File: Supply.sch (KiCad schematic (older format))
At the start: 27 parts, among them IC1 LM5017, IC2 AP65111, U6 7805_SO8

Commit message: - removed lots of unused circuitry - implemented new DMOS power stage - power supplies still missing - removed rescue lib and fixed referenced
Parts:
- removed C10, C45, C48: 22u, Capacitor_SMD:C_0805_2012Metric, symbol Device:C
- removed C11, C12, C27, C31, C32: 100n, Capacitor_SMD:C_0805_2012Metric, symbol Device:C
- removed C28: 100n, Capacitor_SMD:C_0805_2012Metric, symbol Device:C_Small
- removed C30: 1u, Capacitor_SMD:C_1206_3216Metric, symbol Device:C
- removed C46: 3n3, Capacitor_SMD:C_0805_2012Metric, symbol Device:C_Small
- removed C49: 100u 22V, Capacitor_THT:CP_Radial_D6.3mm_P2.50mm, symbol Device:CP
- removed D8: 4148, Diode_SMD:D_MiniMELF, symbol Device:D_Small
- removed IC1: LM5017, Package_SO:HSOP-8-1EP_3.9x4.9mm_P1.27mm_EP2.41x3.1mm, symbol Revolter-rescue:LM5017
- removed IC2: AP65111, Package_TO_SOT_SMD:SOT-23-6, symbol Revolter-rescue:AP65111
- removed L1: VLS6045EX-221M, Inductor_SMD:L_Taiyo-Yuden_NR-60xx_HandSoldering, symbol Revolter-rescue:INDUCTOR
- removed L2: NRH2410T100MN, Inductor_SMD:L_Taiyo-Yuden_NR-24xx_HandSoldering, symbol Revolter-rescue:INDUCTOR_SMALL
- removed R30: 82k, Resistor_SMD:R_0805_2012Metric, symbol Device:R
- removed R31, R44: 10k, Resistor_SMD:R_0805_2012Metric, symbol Device:R
- removed R39: 499k, Resistor_SMD:R_0805_2012Metric, symbol Device:R
- removed R40: 59k, Resistor_SMD:R_0805_2012Metric, symbol Device:R
- removed R41: 46k4, Resistor_SMD:R_0805_2012Metric, symbol Device:R
- removed R42: 40k2, Resistor_SMD:R_0805_2012Metric, symbol Device:R
- removed R43: 1k, Resistor_SMD:R_0805_2012Metric, symbol Device:R
- removed R49: 13k, Resistor_SMD:R_0805_2012Metric, symbol Device:R
- removed U6: 7805_SO8, Package_SO:SO-8_3.9x4.9mm_P1.27mm, symbol Revolter-rescue:7805_SO8
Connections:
- net labels removed: +12V, +3V3, +5V, +BATT, GND
- wire segments 41 -> 0

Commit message: - fixed ACS730 pin issue - added power supplies - added footprint library - added footprint for IRSM005
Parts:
- added C10, C45, C48: 22u, Capacitor_SMD:C_0805_2012Metric, symbol Device:C
- added C12, C31, C32: 100n, Capacitor_SMD:C_0805_2012Metric, symbol Device:C
- added C28: 100n, Capacitor_SMD:C_0805_2012Metric, symbol Device:C_Small
- added C30: 1u, Capacitor_SMD:C_1206_3216Metric, symbol Device:C
- added C46: 3n3, Capacitor_SMD:C_0805_2012Metric, symbol Device:C_Small
- added C49: 100u 22V, Capacitor_THT:CP_Radial_D6.3mm_P2.50mm, symbol Device:CP
- added D8: 4148, Diode_SMD:D_MiniMELF, symbol Device:D_Small
- added IC1: LM5017, Package_SO:HSOP-8-1EP_3.9x4.9mm_P1.27mm_EP2.41x3.1mm, symbol Regulator_Switching:LM5017MR
- added IC2: AP65111, Package_TO_SOT_SMD:SOT-23-6, symbol Regulator_Switching:AP65111AWU
- added L2: NRH2410T100MN, Inductor_SMD:L_Taiyo-Yuden_NR-24xx_HandSoldering, symbol Device:L_Small
- added L3: VLS6045EX-221M, Inductor_SMD:L_Taiyo-Yuden_NR-60xx, symbol Device:L
- added R30: 82k, Resistor_SMD:R_0805_2012Metric, symbol Device:R
- added R31, R44: 10k, Resistor_SMD:R_0805_2012Metric, symbol Device:R
- added R39: 499k, Resistor_SMD:R_0805_2012Metric, symbol Device:R
- added R40: 59k, Resistor_SMD:R_0805_2012Metric, symbol Device:R
- added R41: 46k4, Resistor_SMD:R_0805_2012Metric, symbol Device:R
- added R42: 40k2, Resistor_SMD:R_0805_2012Metric, symbol Device:R
- added R43: 1k, Resistor_SMD:R_0805_2012Metric, symbol Device:R
- added R49: 13k, Resistor_SMD:R_0805_2012Metric, symbol Device:R
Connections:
- new net: C31.1, D8.1 (K), IC1.6 (VCC)
- new net: C28.1, IC1.5 (FB), R43.1, R44.1
- new net: C32.1, IC1.8 (SW), L3.1, R41.2
- new net: C32.2, IC1.7 (BST)
- new net: IC1.3 (ULVO), R30.1, R31.2
- new net: IC1.4 (RON), R39.2
- new net: C28.2, C46.2, R41.1
- new net: C12.1, IC2.3 (SW), L2.1
- new net: C12.2, IC2.4 (BST)
- new net: R40.1, R42.2, R49.1
- new net: IC2.6 (FB), R40.2
- new net +12V: C10.1, C46.1, C48.1, C49.1, D8.2 (A), IC2.1 (IN), IC2.5 (EN), L3.2, R44.2
- new net +3V3: C45.1, L2.2, R42.1
- new net +BATT: C30.1, IC1.2 (VIN), R30.2, R39.1
- new net GND: C10.2, C30.2, C31.2, C45.2, C48.2, C49.2, IC1.1 (RTN), IC1.9 (RTNPAD), IC2.2 (GND), R31.1, R43.2, R49.2

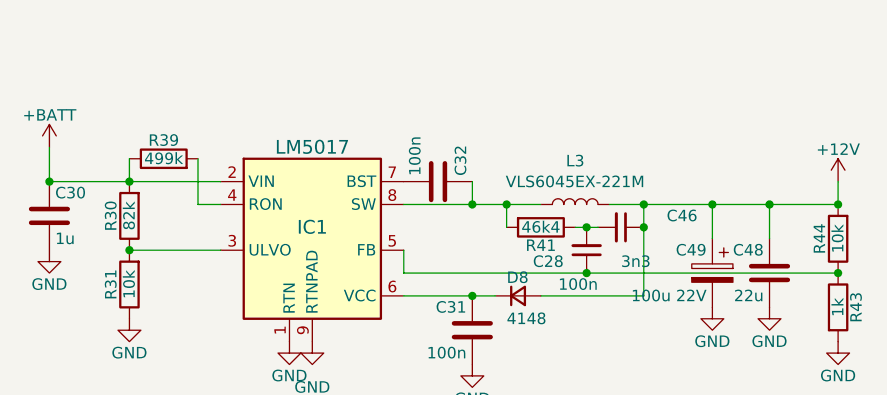
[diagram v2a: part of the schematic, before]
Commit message: - added temp sensors and fan/pump outputs - made footprint selection
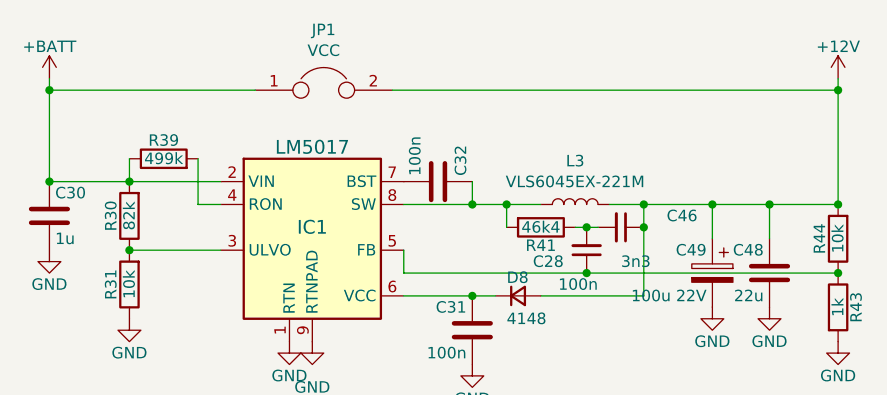
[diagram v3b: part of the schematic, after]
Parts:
- added JP1: VCC, Jumper:SolderJumper-2_P1.3mm_Open_TrianglePad1.0x1.5mm, symbol Device:Jumper
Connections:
- net +12V: now also JP1.2
- net +BATT: now also JP1.1
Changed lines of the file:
@@
 $Descr A4 11693 8268
 encoding utf-8
-Sheet 3 4
+Sheet 2 4
 Title ""
 Date ""
@@
 L power:+12V #PWR052
 U 1 1 5757C6C9
-P 7350 1450
-F 0 "#PWR052" H 7350 1300 50  0001 C CNN
-F 1 "+12V" H 7350 1590 50  0000 C CNN
-F 2 "" H 7350 1450 60  0000 C CNN
-F 3 "" H 7350 1450 60  0000 C CNN
-	1    7350 1450
+P 7350 1000
+F 0 "#PWR052" H 7350 850 50  0001 C CNN
+F 1 "+12V" H 7350 1140 50  0000 C CNN
+F 2 "" H 7350 1000 60  0000 C CNN
+F 3 "" H 7350 1000 60  0000 C CNN
+	1    7350 1000
 	1    0    0    -1
 $EndComp
@@
 Connection ~ 7350 1850
 Wire Wire Line
-	7350 1550 7350 1450
+	7350 1550 7350 1050
 Connection ~ 7350 1550
 Wire Wire Line
@@
 L power:+BATT #PWR075
 U 1 1 59C14A31
-P 3900 1300
-F 0 "#PWR075" H 3900 1150 50  0001 C CNN
-F 1 "+BATT" H 3900 1440 50  0000 C CNN
-F 2 "" H 3900 1300 50  0000 C CNN
-F 3 "" H 3900 1300 50  0000 C CNN
-	1    3900 1300
-	1    0    0    -1
-$EndComp
-Wire Wire Line
-	3900 1300 3900 1450
+P 3900 1000
+F 0 "#PWR075" H 3900 850 50  0001 C CNN
+F 1 "+BATT" H 3900 1140 50  0000 C CNN
+F 2 "" H 3900 1000 50  0000 C CNN
+F 3 "" H 3900 1000 50  0000 C CNN
+	1    3900 1000
+	1    0    0    -1
+$EndComp
+Wire Wire Line
+	3900 1000 3900 1050
 $Comp
 L Regulator_Switching:AP65111AWU IC2
@@
 	0    -1   -1   0
 $EndComp
+$Comp
+L Device:Jumper JP1
+U 1 1 5EF36517
+P 5100 1050
+F 0 "JP1" H 5100 1314 50  0000 C CNN
+F 1 "VCC" H 5100 1223 50  0000 C CNN
+F 2 "Jumper:SolderJumper-2_P1.3mm_Open_TrianglePad1.0x1.5mm" H 5100 1050 50  0001 C CNN
+F 3 "~" H 5100 1050 50  0001 C CNN
+	1    5100 1050
+	1    0    0    -1
+$EndComp
+Wire Wire Line
+	3900 1050 4800 1050
+Connection ~ 3900 1050
+Wire Wire Line
+	3900 1050 3900 1450
+Wire Wire Line
+	5400 1050 7350 1050
+Connection ~ 7350 1050
+Wire Wire Line
+	7350 1050 7350 1000
 $EndSCHEMATC

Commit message: - did most of the layout
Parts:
- C30: footprint Capacitor_SMD:C_1206_3216Metric -> Capacitor_SMD:C_0805_2012Metric
- D8: footprint Diode_SMD:D_MiniMELF -> Diode_SMD:D_SOD-123
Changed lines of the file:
@@
 F 0 "C30" H 3925 1700 50  0000 L CNN
 F 1 "1u" H 3925 1500 50  0000 L CNN
-F 2 "Capacitor_SMD:C_1206_3216Metric" H 3938 1450 50  0001 C CNN
+F 2 "Capacitor_SMD:C_0805_2012Metric" H 3938 1450 50  0001 C CNN
 F 3 "" H 3900 1600 50  0000 C CNN
 	1    3900 1600
@@
 Connection ~ 4250 1750
 Connection ~ 4250 1450
-$Comp
-L Device:D_Small D8
-U 1 1 59A220CE
-P 5950 1950
-F 0 "D8" H 5900 2030 50  0000 L CNN
-F 1 "4148" H 5900 1850 50  0000 L CNN
-F 2 "Diode_SMD:D_MiniMELF" V 5950 1950 50  0001 C CNN
-F 3 "" V 5950 1950 50  0000 C CNN
-	1    5950 1950
-	1    0    0    -1
-$EndComp
 Connection ~ 5750 1950
 $Comp
@@
 Wire Wire Line
 	7350 1050 7350 1000
+$Comp
+L Device:D_Small D8
+U 1 1 59A220CE
+P 5950 1950
+F 0 "D8" H 5900 2030 50  0000 L CNN
+F 1 "4148" H 5900 1850 50  0000 L CNN
+F 2 "Diode_SMD:D_SOD-123" V 5950 1950 50  0001 C CNN
+F 3 "" V 5950 1950 50  0000 C CNN
+	1    5950 1950
+	1    0    0    -1
+$EndComp
 $EndSCHEMATC

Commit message: - replaced L2 by 0805 coil - added a load of DC link caps - finalized layout
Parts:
- L2: footprint Inductor_SMD:L_Taiyo-Yuden_NR-24xx_HandSoldering -> Inductor_SMD:L_0805_2012Metric
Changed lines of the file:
@@
 F 0 "L2" V 6000 3600 50  0000 C CNN
 F 1 "NRH2410T100MN" V 6100 3450 50  0000 C CNN
-F 2 "Inductor_SMD:L_Taiyo-Yuden_NR-24xx_HandSoldering" H 5950 3600 50  0001 C CNN
+F 2 "Inductor_SMD:L_0805_2012Metric" H 5950 3600 50  0001 C CNN
 F 3 "" H 5950 3600 50  0000 C CNN
 	1    5950 3600

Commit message: - changed current sensors - updated symbols - exported for production
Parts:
- C49: symbol Device:CP -> Device:C_Polarized
- JP1: symbol Device:Jumper -> Jumper:SolderJumper_2_Open
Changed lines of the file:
@@
 $EndComp
 $Comp
-L Device:CP C49
+L Device:C_Polarized C49
 U 1 1 589C2A67
 P 6800 1850
@@
 $EndComp
 $Comp
-L Device:Jumper JP1
+L Jumper:SolderJumper_2_Open JP1
 U 1 1 5EF36517
-P 5100 1050
-F 0 "JP1" H 5100 1314 50  0000 C CNN
-F 1 "VCC" H 5100 1223 50  0000 C CNN
-F 2 "Jumper:SolderJumper-2_P1.3mm_Open_TrianglePad1.0x1.5mm" H 5100 1050 50  0001 C CNN
-F 3 "~" H 5100 1050 50  0001 C CNN
-	1    5100 1050
-	1    0    0    -1
-$EndComp
-Wire Wire Line
-	3900 1050 4800 1050
+P 5050 1050
+F 0 "JP1" H 5050 1314 50  0000 C CNN
+F 1 "VCC" H 5050 1223 50  0000 C CNN
+F 2 "Jumper:SolderJumper-2_P1.3mm_Open_TrianglePad1.0x1.5mm" H 5050 1050 50  0001 C CNN
+F 3 "~" H 5050 1050 50  0001 C CNN
+	1    5050 1050
+	1    0    0    -1
+$EndComp
+Wire Wire Line
+	3900 1050 4900 1050
 Connection ~ 3900 1050
 Wire Wire Line
 	3900 1050 3900 1450
 Wire Wire Line
-	5400 1050 7350 1050
+	5200 1050 7350 1050
 Connection ~ 7350 1050
 Wire Wire Line

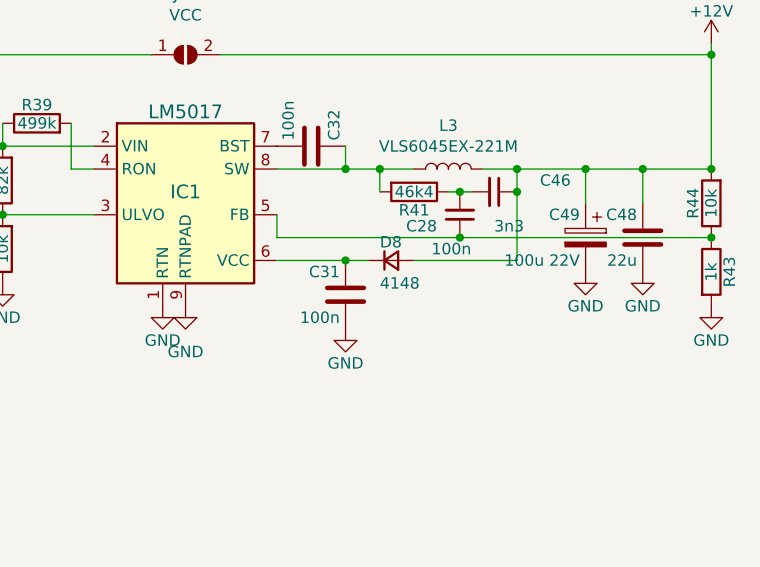
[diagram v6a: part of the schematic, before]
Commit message: - added flyback diodes to FAN outputs - added fourth DC cap - changed TEMP3 to motor temp
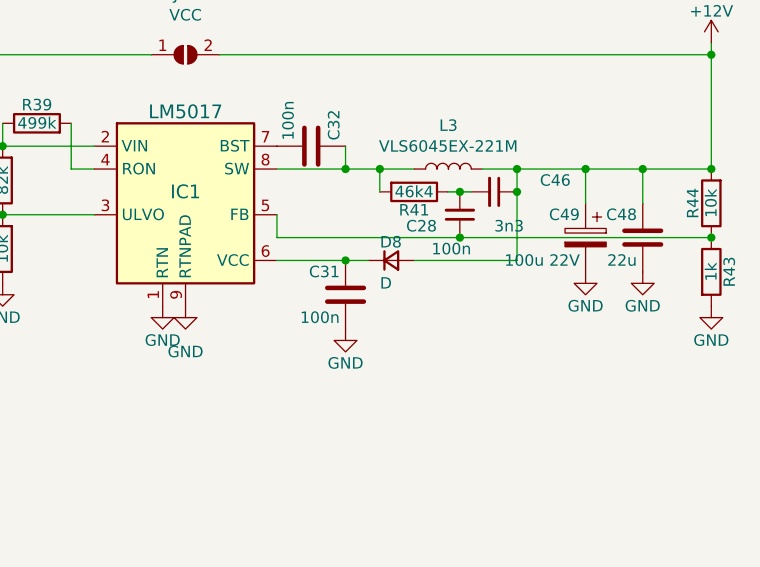
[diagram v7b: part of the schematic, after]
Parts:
- D8: value 4148 -> D
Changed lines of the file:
@@
 P 5950 1950
 F 0 "D8" H 5900 2030 50  0000 L CNN
-F 1 "4148" H 5900 1850 50  0000 L CNN
+F 1 "D" H 5900 1850 50  0000 L CNN
 F 2 "Diode_SMD:D_SOD-123" V 5950 1950 50  0001 C CNN
 F 3 "" V 5950 1950 50  0000 C CNN

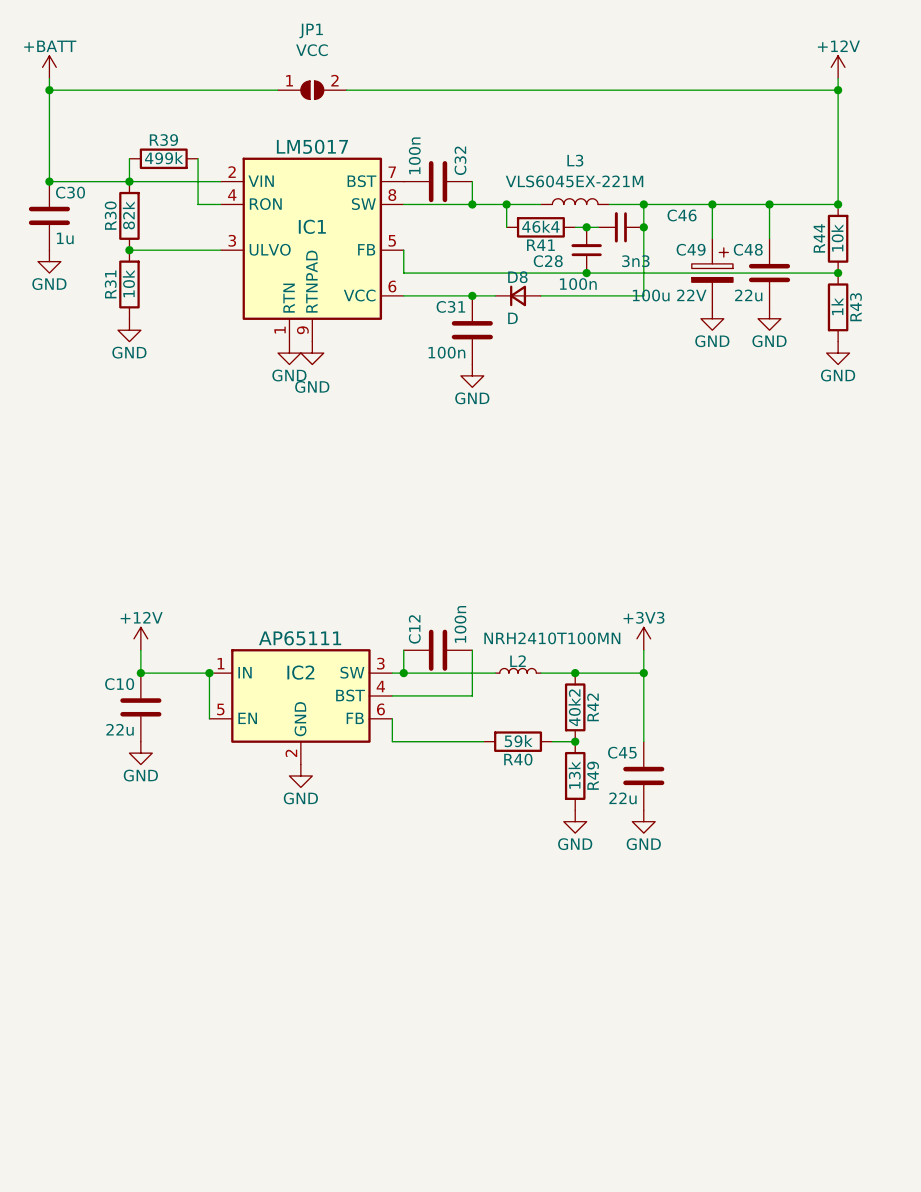
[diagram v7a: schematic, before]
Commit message: - removed one fan output - moved PWM pins to TIM4 - added pull-up to fan output (for 4pin fan) - removed blue power LED - split 12pin to 5 2pin connectors - reduced LED resistors - removed optional current sensor - removed HV DCDC converter - added some cap values
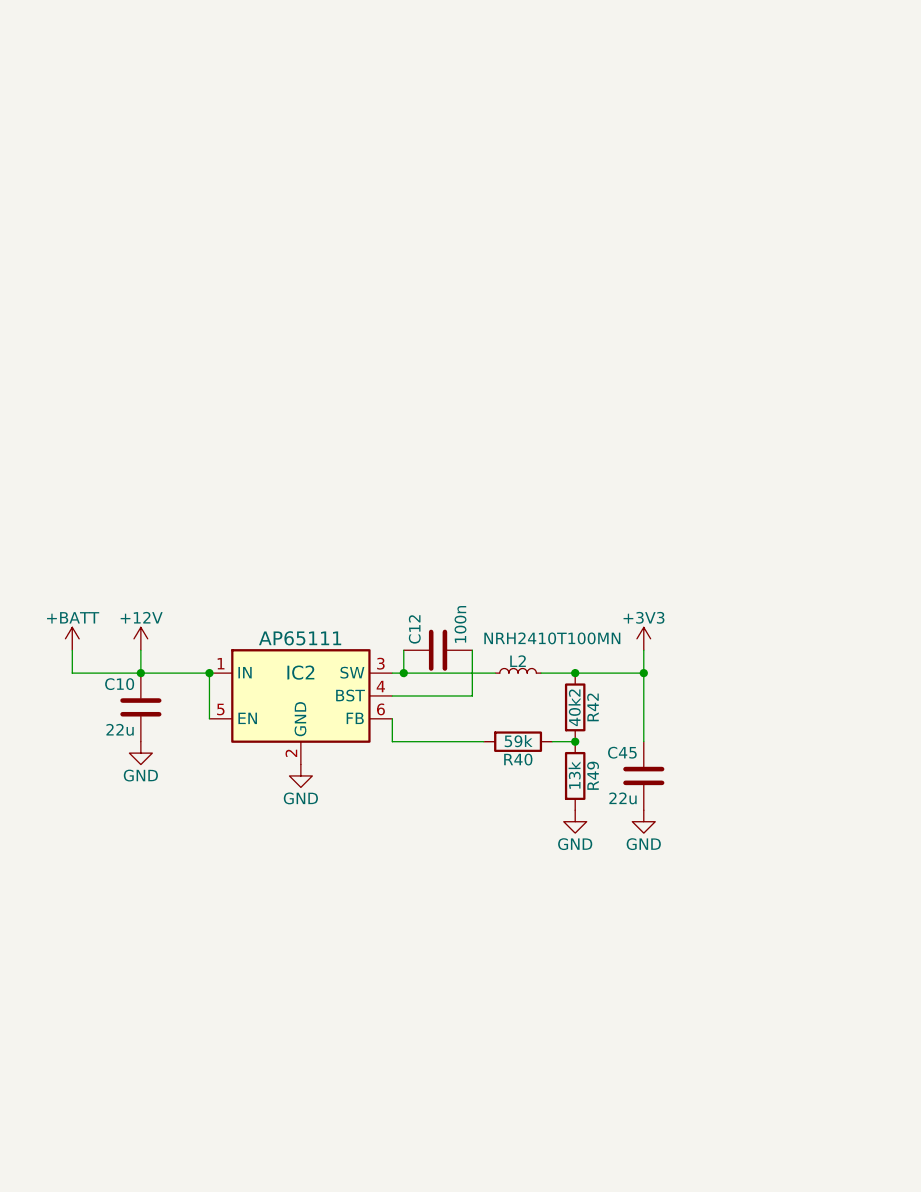
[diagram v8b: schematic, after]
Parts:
- removed C28: 100n, Capacitor_SMD:C_0805_2012Metric, symbol Device:C_Small
- removed C30: 1u, Capacitor_SMD:C_0805_2012Metric, symbol Device:C
- removed C31, C32: 100n, Capacitor_SMD:C_0805_2012Metric, symbol Device:C
- removed C46: 3n3, Capacitor_SMD:C_0805_2012Metric, symbol Device:C_Small
- removed C48: 22u, Capacitor_SMD:C_0805_2012Metric, symbol Device:C
- removed C49: 100u 22V, Capacitor_THT:CP_Radial_D6.3mm_P2.50mm, symbol Device:C_Polarized
- removed D8: D, Diode_SMD:D_SOD-123, symbol Device:D_Small
- removed IC1: LM5017, Package_SO:HSOP-8-1EP_3.9x4.9mm_P1.27mm_EP2.41x3.1mm, symbol Regulator_Switching:LM5017MR
- removed JP1: VCC, Jumper:SolderJumper-2_P1.3mm_Open_TrianglePad1.0x1.5mm, symbol Jumper:SolderJumper_2_Open
- removed L3: VLS6045EX-221M, Inductor_SMD:L_Taiyo-Yuden_NR-60xx, symbol Device:L
- removed R30: 82k, Resistor_SMD:R_0805_2012Metric, symbol Device:R
- removed R31, R44: 10k, Resistor_SMD:R_0805_2012Metric, symbol Device:R
- removed R39: 499k, Resistor_SMD:R_0805_2012Metric, symbol Device:R
- removed R41: 46k4, Resistor_SMD:R_0805_2012Metric, symbol Device:R
- removed R43: 1k, Resistor_SMD:R_0805_2012Metric, symbol Device:R
